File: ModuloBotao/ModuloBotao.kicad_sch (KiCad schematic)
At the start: 8 parts, among them J1001 Pin, J1002 Bt_ext, SW1001 Button

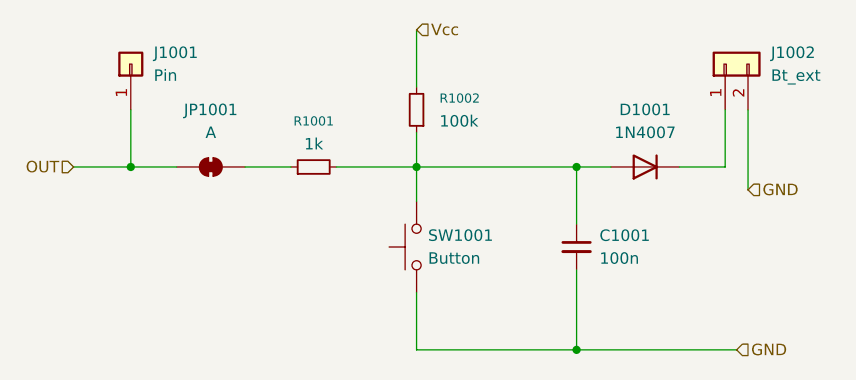
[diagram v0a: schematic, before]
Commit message: Completed circuit.
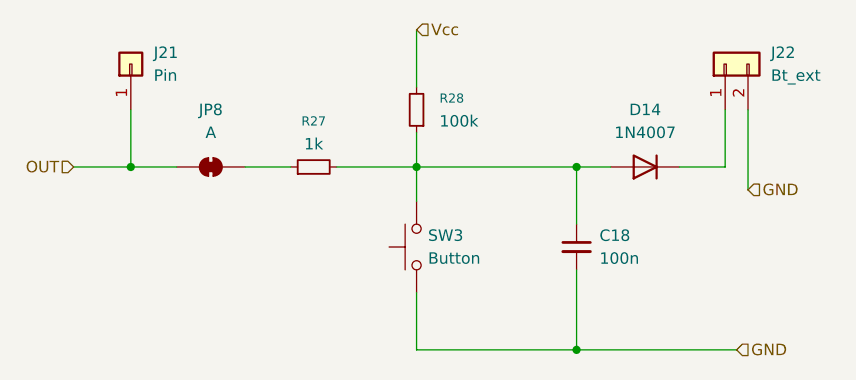
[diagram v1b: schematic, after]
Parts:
- renumbered C1001 to C18, D1001 to D14, J1001 to J21, J1002 to J22, JP1001 to JP8, R1001 to R27, R1002 to R28, SW1001 to SW3
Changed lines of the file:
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@@
 		(dnp no)
 		(fields_autoplaced yes)
-		(property "Reference" "J1001"
+		(property "Reference" "J21"
 			(at 102.87 68.5799 90)
 			(effects
@@
 		)
 		(instances
-			(project ""
-				(path "/774e0363-35a9-4faf-821b-f445a1f461c7"
-					(reference "J1001")
+			(project "Arduino"
+				(path "/b1260de1-9c48-4b08-a759-f31e40d6183e/76c98e6a-1d6c-4f25-8a72-613bfa81c9a8"
+					(reference "J21")
+					(unit 1)
+				)
+				(path "/b1260de1-9c48-4b08-a759-f31e40d6183e/d6d2074d-a8e9-4707-be31-4e7eef2e7c42"
+					(reference "J19")
 					(unit 1)
 				)
@@
 		(dnp no)
 		(fields_autoplaced yes)
-		(property "Reference" "D1001"
+		(property "Reference" "D14"
 			(at 157.48 74.93 0)
 			(effects
@@
 		)
 		(instances
-			(project ""
-				(path "/774e0363-35a9-4faf-821b-f445a1f461c7"
-					(reference "D1001")
+			(project "Arduino"
+				(path "/b1260de1-9c48-4b08-a759-f31e40d6183e/76c98e6a-1d6c-4f25-8a72-613bfa81c9a8"
+					(reference "D14")
+					(unit 1)
+				)
+				(path "/b1260de1-9c48-4b08-a759-f31e40d6183e/d6d2074d-a8e9-4707-be31-4e7eef2e7c42"
+					(reference "D13")
 					(unit 1)
 				)
@@
 		(dnp no)
 		(fields_autoplaced yes)
-		(property "Reference" "R1002"
+		(property "Reference" "R28"
 			(at 134.62 73.6599 0)
 			(effects
@@
 		)
 		(instances
-			(project "ModuloBotao"
-				(path "/774e0363-35a9-4faf-821b-f445a1f461c7"
-					(reference "R1002")
+			(project "Arduino"
+				(path "/b1260de1-9c48-4b08-a759-f31e40d6183e/76c98e6a-1d6c-4f25-8a72-613bfa81c9a8"
+					(reference "R28")
+					(unit 1)
+				)
+				(path "/b1260de1-9c48-4b08-a759-f31e40d6183e/d6d2074d-a8e9-4707-be31-4e7eef2e7c42"
+					(reference "R26")
 					(unit 1)
 				)
@@
 		(dnp no)
 		(fields_autoplaced yes)
-		(property "Reference" "R1001"
+		(property "Reference" "R27"
 			(at 120.65 76.2 90)
 			(effects
@@
 		)
 		(instances
-			(project ""
-				(path "/774e0363-35a9-4faf-821b-f445a1f461c7"
-					(reference "R1001")
+			(project "Arduino"
+				(path "/b1260de1-9c48-4b08-a759-f31e40d6183e/76c98e6a-1d6c-4f25-8a72-613bfa81c9a8"
+					(reference "R27")
+					(unit 1)
+				)
+				(path "/b1260de1-9c48-4b08-a759-f31e40d6183e/d6d2074d-a8e9-4707-be31-4e7eef2e7c42"
+					(reference "R25")
 					(unit 1)
 				)
@@
 		(dnp no)
 		(fields_autoplaced yes)
-		(property "Reference" "JP1001"
+		(property "Reference" "JP8"
 			(at 109.22 74.93 0)
 			(effects
@@
 		)
 		(instances
-			(project ""
-				(path "/774e0363-35a9-4faf-821b-f445a1f461c7"
-					(reference "JP1001")
+			(project "Arduino"
+				(path "/b1260de1-9c48-4b08-a759-f31e40d6183e/76c98e6a-1d6c-4f25-8a72-613bfa81c9a8"
+					(reference "JP8")
+					(unit 1)
+				)
+				(path "/b1260de1-9c48-4b08-a759-f31e40d6183e/d6d2074d-a8e9-4707-be31-4e7eef2e7c42"
+					(reference "JP7")
 					(unit 1)
 				)
@@
 		(dnp no)
 		(fields_autoplaced yes)
-		(property "Reference" "SW1001"
+		(property "Reference" "SW3"
 			(at 133.35 88.8999 90)
 			(effects
@@
 		)
 		(instances
-			(project ""
-				(path "/774e0363-35a9-4faf-821b-f445a1f461c7"
-					(reference "SW1001")
+			(project "Arduino"
+				(path "/b1260de1-9c48-4b08-a759-f31e40d6183e/76c98e6a-1d6c-4f25-8a72-613bfa81c9a8"
+					(reference "SW3")
+					(unit 1)
+				)
+				(path "/b1260de1-9c48-4b08-a759-f31e40d6183e/d6d2074d-a8e9-4707-be31-4e7eef2e7c42"
+					(reference "SW2")
 					(unit 1)
 				)
@@
 		(dnp no)
 		(fields_autoplaced yes)
-		(property "Reference" "C1001"
+		(property "Reference" "C18"
 			(at 152.4 88.9062 0)
 			(effects
@@
 		)
 		(instances
-			(project ""
-				(path "/774e0363-35a9-4faf-821b-f445a1f461c7"
-					(reference "C1001")
+			(project "Arduino"
+				(path "/b1260de1-9c48-4b08-a759-f31e40d6183e/76c98e6a-1d6c-4f25-8a72-613bfa81c9a8"
+					(reference "C18")
+					(unit 1)
+				)
+				(path "/b1260de1-9c48-4b08-a759-f31e40d6183e/d6d2074d-a8e9-4707-be31-4e7eef2e7c42"
+					(reference "C17")
 					(unit 1)
 				)
@@
 		(dnp no)
 		(fields_autoplaced yes)
-		(property "Reference" "J1002"
+		(property "Reference" "J22"
 			(at 171.45 68.5799 90)
 			(effects
@@
 		)
 		(instances
-			(project ""
-				(path "/774e0363-35a9-4faf-821b-f445a1f461c7"
-					(reference "J1002")
-					(unit 1)
-				)
-			)
-		)
-	)
-	(sheet_instances
-		(path "/"
-			(page "1")
-		)
-	)
-	(embedded_fonts no)
+			(project "Arduino"
+				(path "/b1260de1-9c48-4b08-a759-f31e40d6183e/76c98e6a-1d6c-4f25-8a72-613bfa81c9a8"
+					(reference "J22")
+					(unit 1)
+				)
+				(path "/b1260de1-9c48-4b08-a759-f31e40d6183e/d6d2074d-a8e9-4707-be31-4e7eef2e7c42"
+					(reference "J20")
+					(unit 1)
+				)
+			)
+		)
+	)
 )

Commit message: Added all components to arduino pcb.
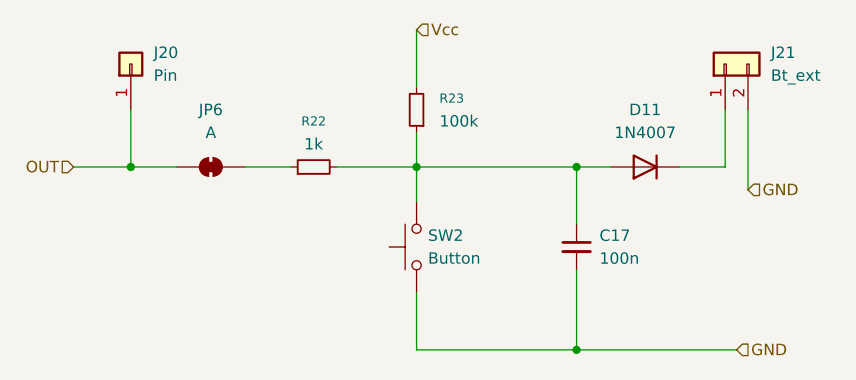
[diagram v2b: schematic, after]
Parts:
- C17: renamed from C18; footprint Capacitor_SMD:C_0805_2012Metric -> Capacitor_SMD:C_0805_2012Metric_Pad1.18x1.45mm_HandSolder
- R22: renamed from R27; footprint Resistor_SMD:R_0805_2012Metric -> Resistor_SMD:R_0805_2012Metric_Pad1.20x1.40mm_HandSolder
- R23: renamed from R28; footprint Resistor_SMD:R_0805_2012Metric -> Resistor_SMD:R_0805_2012Metric_Pad1.20x1.40mm_HandSolder
- renumbered D14 to D11, J21 to J20, J22 to J21, JP8 to JP6, SW3 to SW2
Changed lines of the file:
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@@
 		(dnp no)
 		(fields_autoplaced yes)
-		(property "Reference" "J21"
+		(property "Reference" "J20"
 			(at 102.87 68.5799 90)
 			(effects
@@
 			(project "Arduino"
 				(path "/b1260de1-9c48-4b08-a759-f31e40d6183e/76c98e6a-1d6c-4f25-8a72-613bfa81c9a8"
-					(reference "J21")
-					(unit 1)
-				)
-				(path "/b1260de1-9c48-4b08-a759-f31e40d6183e/d6d2074d-a8e9-4707-be31-4e7eef2e7c42"
-					(reference "J19")
+					(reference "J20")
+					(unit 1)
+				)
+				(path "/b1260de1-9c48-4b08-a759-f31e40d6183e/d6d2074d-a8e9-4707-be31-4e7eef2e7c42"
+					(reference "J22")
 					(unit 1)
 				)
@@
 		(dnp no)
 		(fields_autoplaced yes)
-		(property "Reference" "D14"
+		(property "Reference" "D11"
 			(at 157.48 74.93 0)
 			(effects
@@
 			(project "Arduino"
 				(path "/b1260de1-9c48-4b08-a759-f31e40d6183e/76c98e6a-1d6c-4f25-8a72-613bfa81c9a8"
-					(reference "D14")
-					(unit 1)
-				)
-				(path "/b1260de1-9c48-4b08-a759-f31e40d6183e/d6d2074d-a8e9-4707-be31-4e7eef2e7c42"
-					(reference "D13")
+					(reference "D11")
+					(unit 1)
+				)
+				(path "/b1260de1-9c48-4b08-a759-f31e40d6183e/d6d2074d-a8e9-4707-be31-4e7eef2e7c42"
+					(reference "D12")
 					(unit 1)
 				)
@@
 		(dnp no)
 		(fields_autoplaced yes)
-		(property "Reference" "R28"
+		(property "Reference" "R23"
 			(at 134.62 73.6599 0)
 			(effects
@@
 			)
 		)
-		(property "Footprint" "Resistor_SMD:R_0805_2012Metric"
+		(property "Footprint" "Resistor_SMD:R_0805_2012Metric_Pad1.20x1.40mm_HandSolder"
 			(at 132.08 74.93 0)
 			(effects
@@
 			(project "Arduino"
 				(path "/b1260de1-9c48-4b08-a759-f31e40d6183e/76c98e6a-1d6c-4f25-8a72-613bfa81c9a8"
-					(reference "R28")
-					(unit 1)
-				)
-				(path "/b1260de1-9c48-4b08-a759-f31e40d6183e/d6d2074d-a8e9-4707-be31-4e7eef2e7c42"
-					(reference "R26")
+					(reference "R23")
+					(unit 1)
+				)
+				(path "/b1260de1-9c48-4b08-a759-f31e40d6183e/d6d2074d-a8e9-4707-be31-4e7eef2e7c42"
+					(reference "R25")
 					(unit 1)
 				)
@@
 		(dnp no)
 		(fields_autoplaced yes)
-		(property "Reference" "R27"
+		(property "Reference" "R22"
 			(at 120.65 76.2 90)
 			(effects
@@
 			)
 		)
-		(property "Footprint" "Resistor_SMD:R_0805_2012Metric"
+		(property "Footprint" "Resistor_SMD:R_0805_2012Metric_Pad1.20x1.40mm_HandSolder"
 			(at 120.65 81.28 0)
 			(effects
@@
 			(project "Arduino"
 				(path "/b1260de1-9c48-4b08-a759-f31e40d6183e/76c98e6a-1d6c-4f25-8a72-613bfa81c9a8"
-					(reference "R27")
-					(unit 1)
-				)
-				(path "/b1260de1-9c48-4b08-a759-f31e40d6183e/d6d2074d-a8e9-4707-be31-4e7eef2e7c42"
-					(reference "R25")
+					(reference "R22")
+					(unit 1)
+				)
+				(path "/b1260de1-9c48-4b08-a759-f31e40d6183e/d6d2074d-a8e9-4707-be31-4e7eef2e7c42"
+					(reference "R24")
 					(unit 1)
 				)
@@
 		(dnp no)
 		(fields_autoplaced yes)
-		(property "Reference" "JP8"
+		(property "Reference" "JP6"
 			(at 109.22 74.93 0)
 			(effects
@@
 			(project "Arduino"
 				(path "/b1260de1-9c48-4b08-a759-f31e40d6183e/76c98e6a-1d6c-4f25-8a72-613bfa81c9a8"
-					(reference "JP8")
+					(reference "JP6")
 					(unit 1)
 				)
@@
 		(dnp no)
 		(fields_autoplaced yes)
-		(property "Reference" "SW3"
+		(property "Reference" "SW2"
 			(at 133.35 88.8999 90)
 			(effects
@@
 			(project "Arduino"
 				(path "/b1260de1-9c48-4b08-a759-f31e40d6183e/76c98e6a-1d6c-4f25-8a72-613bfa81c9a8"
+					(reference "SW2")
+					(unit 1)
+				)
+				(path "/b1260de1-9c48-4b08-a759-f31e40d6183e/d6d2074d-a8e9-4707-be31-4e7eef2e7c42"
 					(reference "SW3")
-					(unit 1)
-				)
-				(path "/b1260de1-9c48-4b08-a759-f31e40d6183e/d6d2074d-a8e9-4707-be31-4e7eef2e7c42"
-					(reference "SW2")
 					(unit 1)
 				)
@@
 		(dnp no)
 		(fields_autoplaced yes)
-		(property "Reference" "C18"
+		(property "Reference" "C17"
 			(at 152.4 88.9062 0)
 			(effects
@@
 			)
 		)
-		(property "Footprint" "Capacitor_SMD:C_0805_2012Metric"
+		(property "Footprint" "Capacitor_SMD:C_0805_2012Metric_Pad1.18x1.45mm_HandSolder"
 			(at 149.86 90.17 0)
 			(effects
@@
 			(project "Arduino"
 				(path "/b1260de1-9c48-4b08-a759-f31e40d6183e/76c98e6a-1d6c-4f25-8a72-613bfa81c9a8"
+					(reference "C17")
+					(unit 1)
+				)
+				(path "/b1260de1-9c48-4b08-a759-f31e40d6183e/d6d2074d-a8e9-4707-be31-4e7eef2e7c42"
 					(reference "C18")
-					(unit 1)
-				)
-				(path "/b1260de1-9c48-4b08-a759-f31e40d6183e/d6d2074d-a8e9-4707-be31-4e7eef2e7c42"
-					(reference "C17")
 					(unit 1)
 				)
@@
 		(dnp no)
 		(fields_autoplaced yes)
-		(property "Reference" "J22"
+		(property "Reference" "J21"
 			(at 171.45 68.5799 90)
 			(effects
@@
 			(project "Arduino"
 				(path "/b1260de1-9c48-4b08-a759-f31e40d6183e/76c98e6a-1d6c-4f25-8a72-613bfa81c9a8"
-					(reference "J22")
-					(unit 1)
-				)
-				(path "/b1260de1-9c48-4b08-a759-f31e40d6183e/d6d2074d-a8e9-4707-be31-4e7eef2e7c42"
-					(reference "J20")
-					(unit 1)
-				)
+					(reference "J21")
+					(unit 1)
+				)
+				(path "/b1260de1-9c48-4b08-a759-f31e40d6183e/d6d2074d-a8e9-4707-be31-4e7eef2e7c42"
+					(reference "J23")
+					(unit 1)
+				)

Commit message: First version from PCB schematic.
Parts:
- renumbered JP6 to JP7
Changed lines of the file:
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@@
 		(dnp no)
 		(fields_autoplaced yes)
-		(property "Reference" "JP6"
+		(property "Reference" "JP7"
 			(at 109.22 74.93 0)
 			(effects
@@
 			(project "Arduino"
 				(path "/b1260de1-9c48-4b08-a759-f31e40d6183e/76c98e6a-1d6c-4f25-8a72-613bfa81c9a8"
-					(reference "JP6")
+					(reference "JP7")
 					(unit 1)
 				)
 				(path "/b1260de1-9c48-4b08-a759-f31e40d6183e/d6d2074d-a8e9-4707-be31-4e7eef2e7c42"
-					(reference "JP7")
+					(reference "JP8")
 					(unit 1)
 				)
